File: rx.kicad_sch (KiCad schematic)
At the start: 57 parts, among them J7 SMA, Q1 PMOS, Q4 2NPN, T1 RF_BALUN, T1 RXIF_BALUN, U14 MAX2120, U16 DPDT

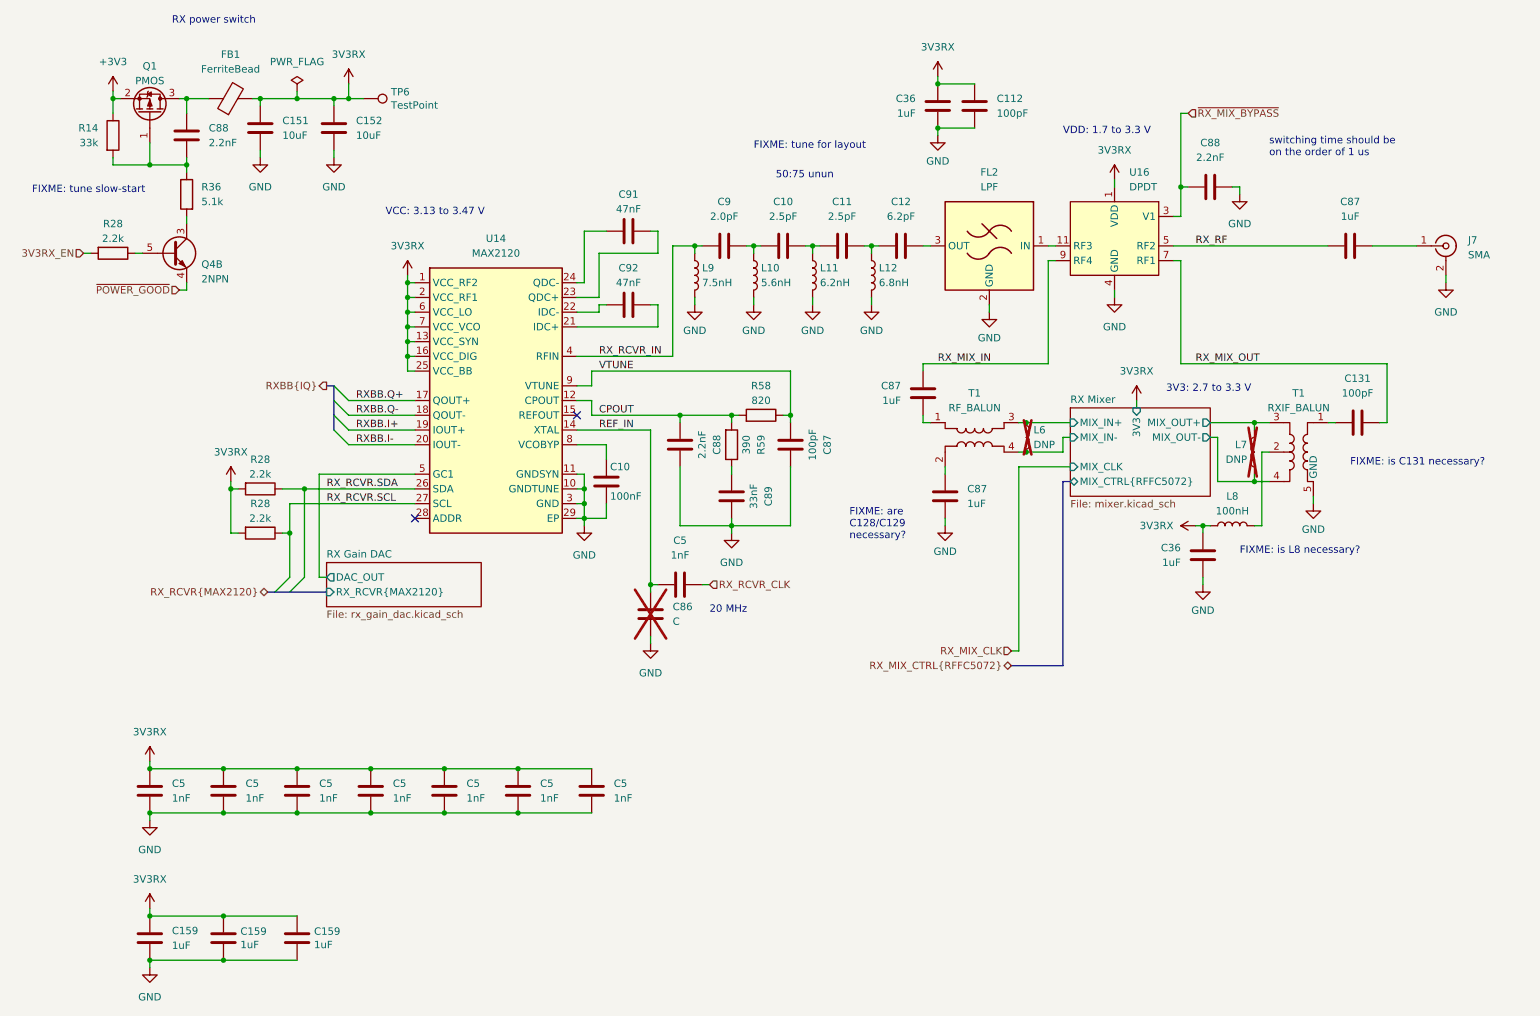
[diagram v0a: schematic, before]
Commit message: add regulator for analog 3.3 V supply
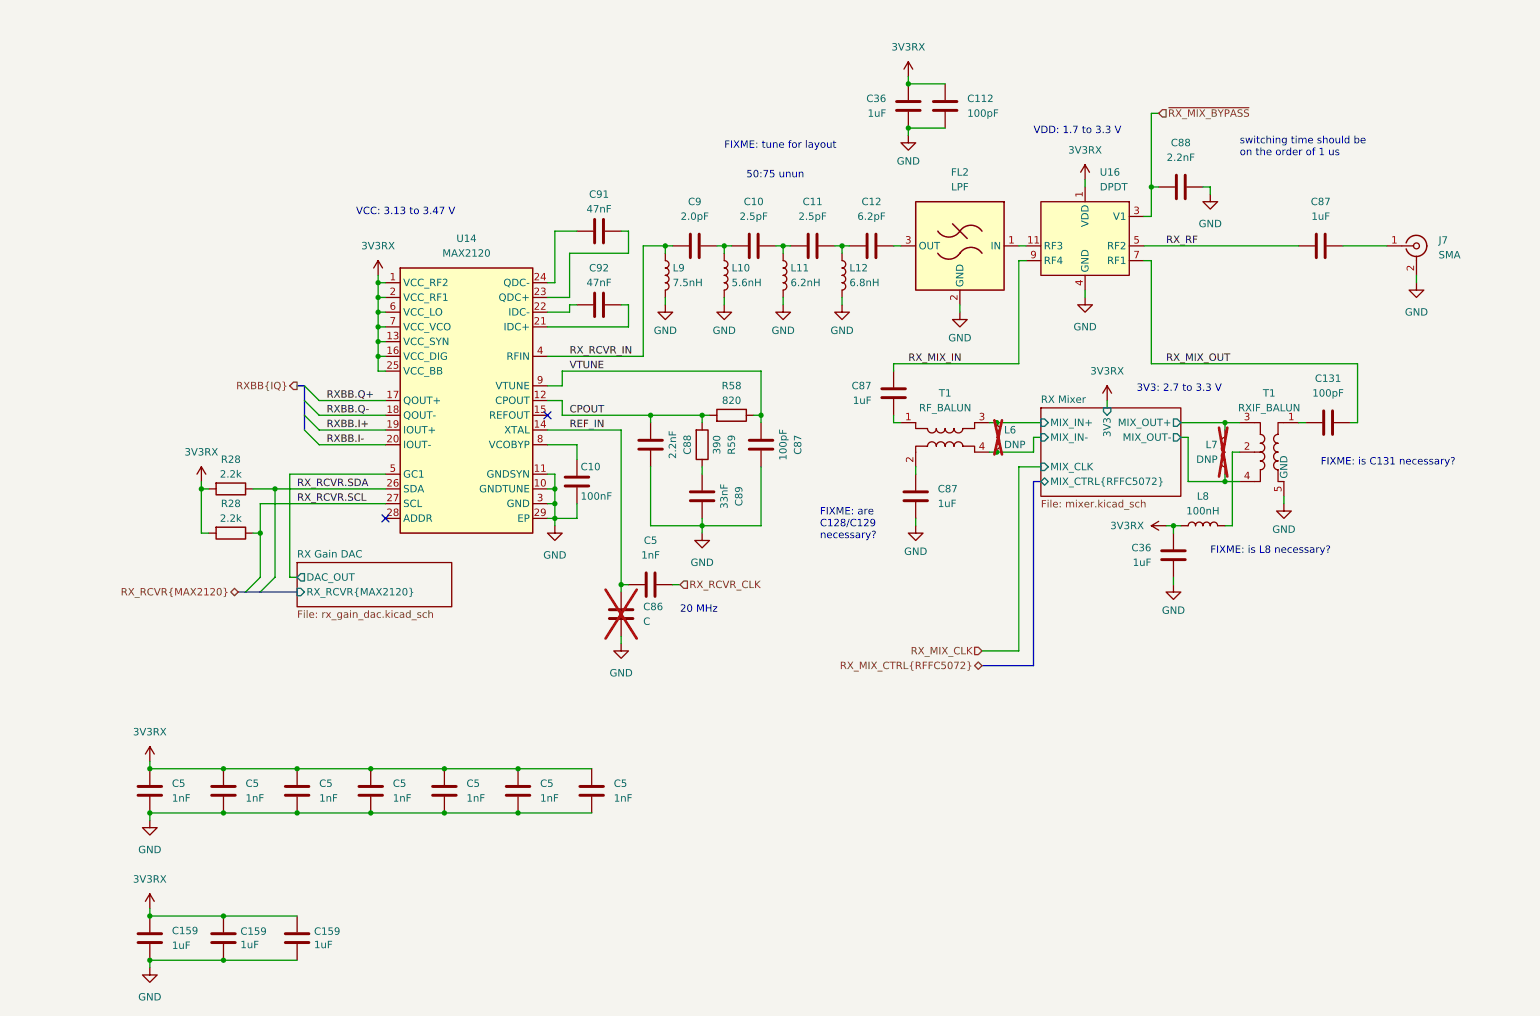
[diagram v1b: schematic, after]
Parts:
- removed C151, C152: 10uF, Capacitor_SMD:C_0603_1608Metric, symbol Device:C
- removed C88: 2.2nF, Capacitor_SMD:C_0201_0603Metric, symbol Device:C
- removed FB1: FerriteBead, symbol Device:FerriteBead
- removed Q1: PMOS, Package_TO_SOT_SMD:SOT-23-3, symbol Device:Q_PMOS_GSD
- removed Q4: 2NPN, Package_TO_SOT_SMD:SOT-363_SC-70-6, symbol Transistor_BJT:BC847BS
- removed R14: 33k, Resistor_SMD:R_0402_1005Metric, symbol Device:R
- removed R28: 2.2k, Resistor_SMD:R_0402_1005Metric, symbol Device:R
- removed R36: 5.1k, Resistor_SMD:R_0402_1005Metric, symbol Device:R
- removed TP6: TestPoint, TestPoint:TestPoint_Pad_D1.0mm, symbol Connector:TestPoint
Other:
- note removed: "FIXME: tune slow-start"
- note removed: "RX power switch"
- moved on the sheet: C10, C11, C112, C12, C131, C36, C5, C86, C87, C88, C89, C9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

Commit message: add SWH two-way RF test connectors
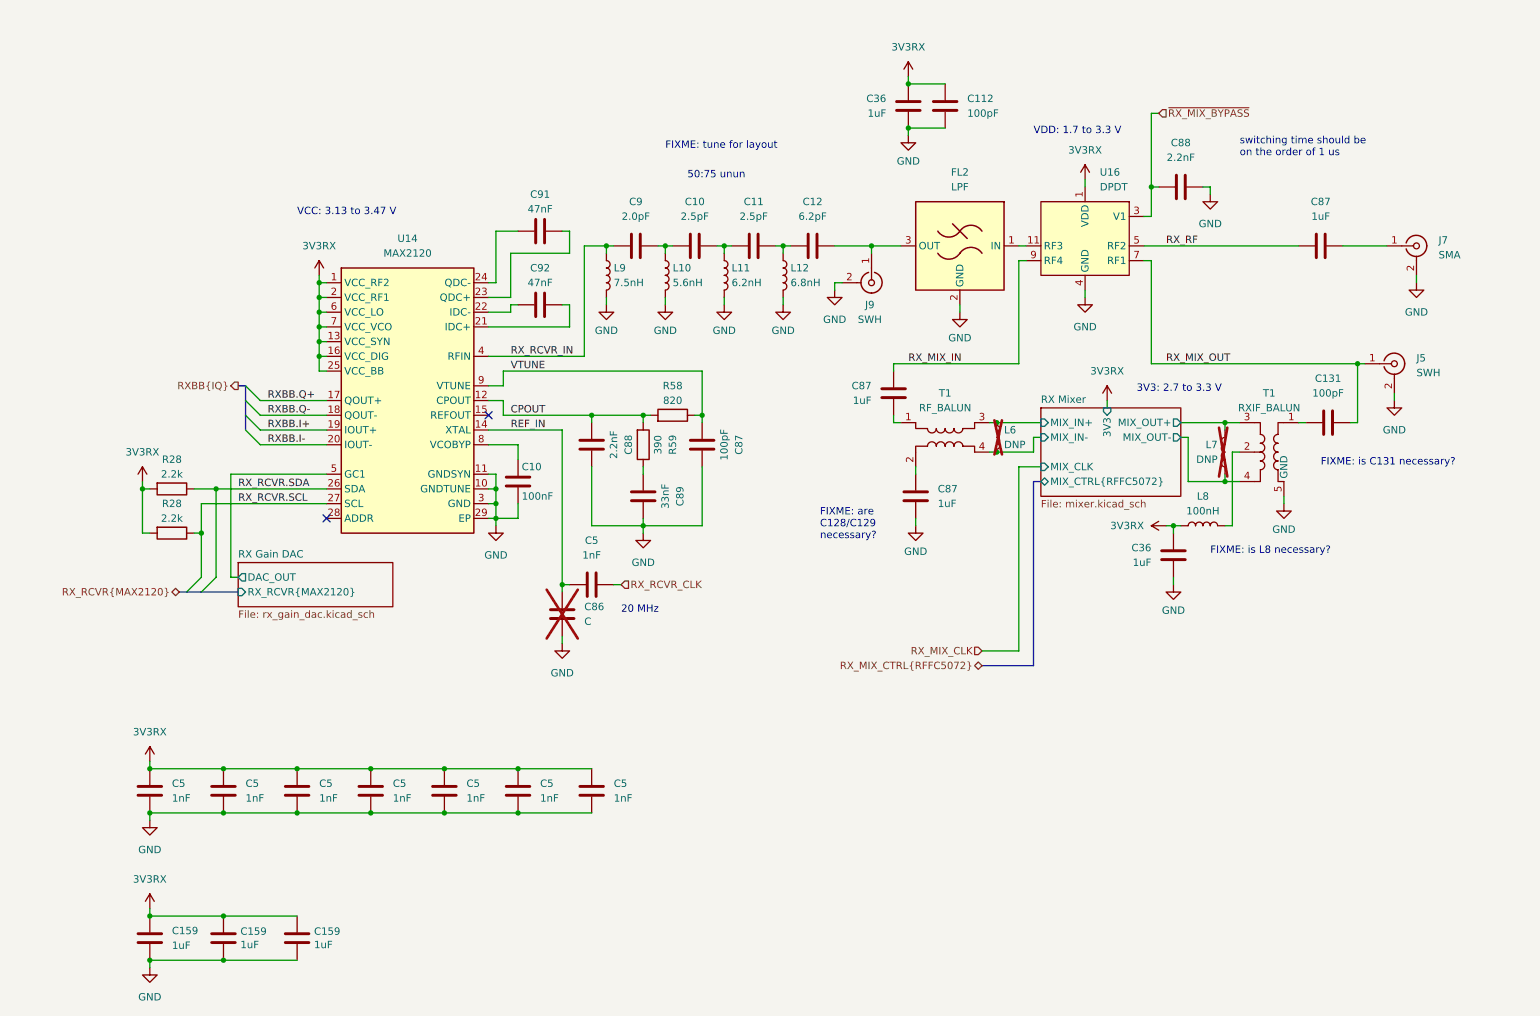
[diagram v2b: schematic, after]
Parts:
- added J5, J9: SWH, symbol Connector:Conn_Coaxial
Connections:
- net GND: now also J5.2 (Ext), J9.2 (Ext)
- net RX_MIX_OUT: now also J5.1 (In)
- net at C12.2, FL2.3 (OUT): now also J9.1 (In)
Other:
- moved on the sheet: C10, C11, C12, C5, C86, C87, C88, C89, C9, C91, C92, L10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

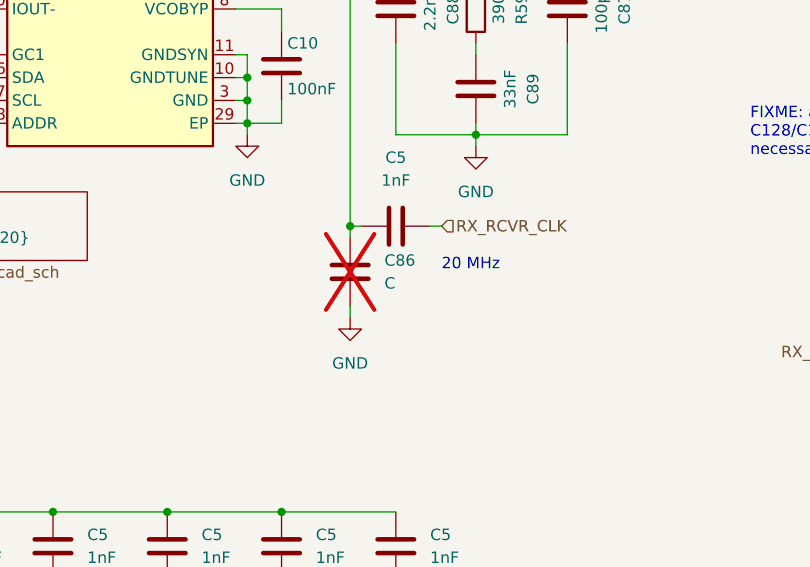
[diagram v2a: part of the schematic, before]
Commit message: update symbol metadata
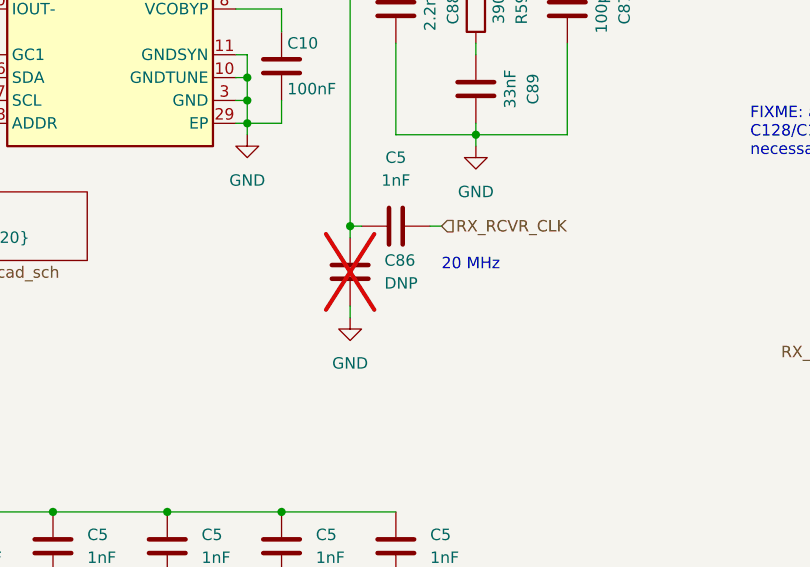
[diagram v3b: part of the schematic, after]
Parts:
- C86: value C -> DNP
- U14: Manufacturer (none) -> Analog Devices; Part Number (none) -> MAX2120CTI+T; Substitution (none) -> MAX2120CTI+
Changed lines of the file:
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@@
       (effects (font (size 1.27 1.27)) (justify left))
     )
-    (property "Value" "C" (at 113.03 121.92 0)
+    (property "Value" "DNP" (at 113.03 121.92 0)
       (effects (font (size 1.27 1.27)) (justify left))
     )
@@
     (property "Datasheet" "https://www.analog.com/media/en/technical-documentation/data-sheets/MAX2120.pdf" (at 82.55 109.22 0)
       (effects (font (size 1.27 1.27) italic) hide)
+    )
+    (property "Manufacturer" "Analog Devices" (at 82.55 83.82 0)
+      (effects (font (size 1.27 1.27)) hide)
+    )
+    (property "Description" "RF RCVR 925MHZ-2.175GHZ 28TQFN" (at 82.55 83.82 0)
+      (effects (font (size 1.27 1.27)) hide)
+    )
+    (property "Part Number" "MAX2120CTI+T" (at 82.55 83.82 0)
+      (effects (font (size 1.27 1.27)) hide)
+    )
+    (property "Substitution" "MAX2120CTI+" (at 82.55 83.82 0)
+      (effects (font (size 1.27 1.27)) hide)
     )
     (pin "1")
@@
       (effects (font (size 1.27 1.27)) hide)
     )
+    (property "Description" "RF FILTER LOW PASS 2.45GHZ 0402" (at 177.8 57.15 0)
+      (effects (font (size 1.27 1.27)) hide)
+    )
     (pin "1")
     (pin "2")
@@
       (effects (font (size 1.27 1.27)) hide)
     )
+    (property "Description" "X-DPDT RF SWITCH" (at 199.39 57.15 0)
+      (effects (font (size 1.27 1.27)) hide)
+    )

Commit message: add SWH connector symbols
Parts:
- removed J5, J9: SWH, symbol Connector:Conn_Coaxial
- added J5, J9: SWH, symbol radio:Conn_Coaxial_MM8930-2620
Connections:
- net GND: now also J5.3 (Ext), J9.3 (Ext)
- net RX_MIX_OUT: now also J5.1 (C); no longer C131.1
- net at C12.2: now also J9.1 (C); no longer FL2.3 (OUT)
- new net: C131.1, J5.2 (R)
- new net: FL2.3 (OUT), J9.2 (R)
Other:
- moved on the sheet: C112, C131, C36, C87, C88, FL2, J7, L6, L7, L8, T1, U16
